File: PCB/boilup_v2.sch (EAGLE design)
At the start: 36 parts, among them IC1 THS4211, J1 USB-MICROB, U1 STM32F0_LQFP64, U2 SPX3819-3.3

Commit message: Added V2 brd layout
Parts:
- removed J1: USB-MICROB, SparkFun-Connectors:USB-MICROB
- removed JP2: (no value), pinhead:PINHD-2X5
- added C4: 100uF, resistor:C-EUC1210K
- added C5: 10uF, resistor:C-EUC0603K
- added H3: MOUNT-HOLE2.8, holes:MOUNT-HOLE2.8
- added JP1: (no value), pinhead:PINHD-1X2
- added LED3: (no value), led:LEDSML0805
- added R12: (no value), resistor:R-US_R0603
- added REDUDNAT: (no value), pinhead:PINHD-2X5
- added U$3: TPSM842, smarttle:TPSM842
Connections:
- removed net D+: J1.D+
- removed net D-: J1.D-
- new net +12V: C5.1, D1.C, JP1.2, MOT.1, U$3.VIN
- new net N$5: LED3.A, R12.1
- net +3V3: no longer IC1G$1.V+
- net +5V: now also C4.1, IC1G$1.V+, REDUDNAT.1, U$3.VOUT; no longer D1.C, J1.VBUS, JP2.1, MOT.1
- net DAC: now also REDUDNAT.3; no longer JP2.3
- net GND: now also C4.2, C5.2, JP1.1, LED3.C, REDUDNAT.10, U$3.GND; no longer J1.GND, JP2.10
- net MOSI: no longer JP2.7
- net PUSH_BUTT: now also R12.2, REDUDNAT.8; no longer JP2.8
- net SCK: no longer JP2.5
- net TIM2_CH3: now also REDUDNAT.9; no longer JP2.9
- net TIM2_CH4: now also REDUDNAT.6; no longer JP2.6
- net USART_RX: now also REDUDNAT.2; no longer JP2.2
- net USART_TX: now also REDUDNAT.4; no longer JP2.4
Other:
- note added: "change to 5?"
- note removed: "POWER AND PORTS"
- moved on the sheet: R1

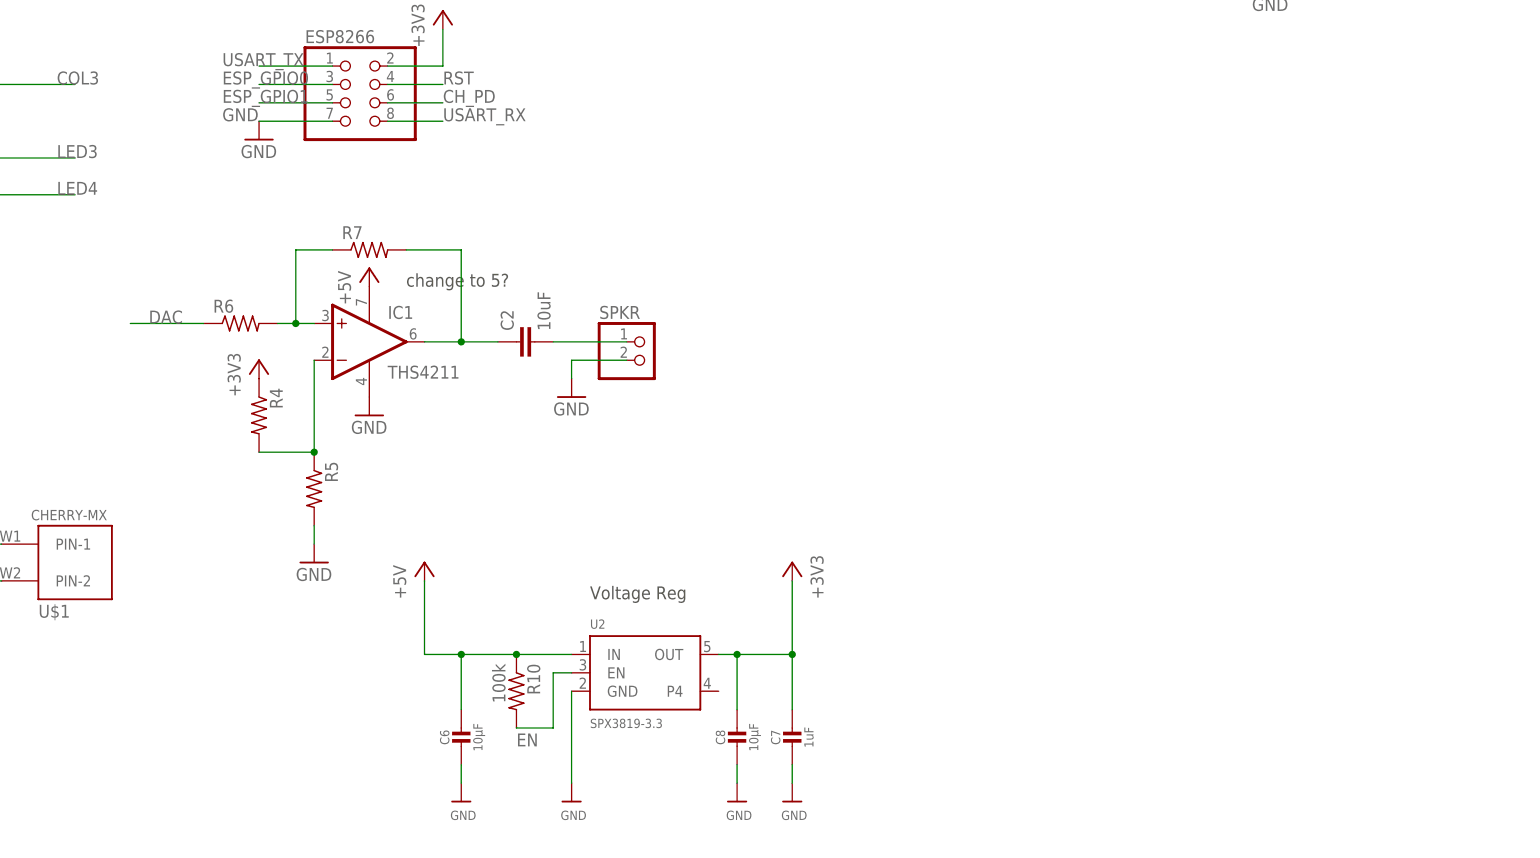
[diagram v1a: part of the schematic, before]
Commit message: replaced speaker circuit, redid board layout. V2 is active development version
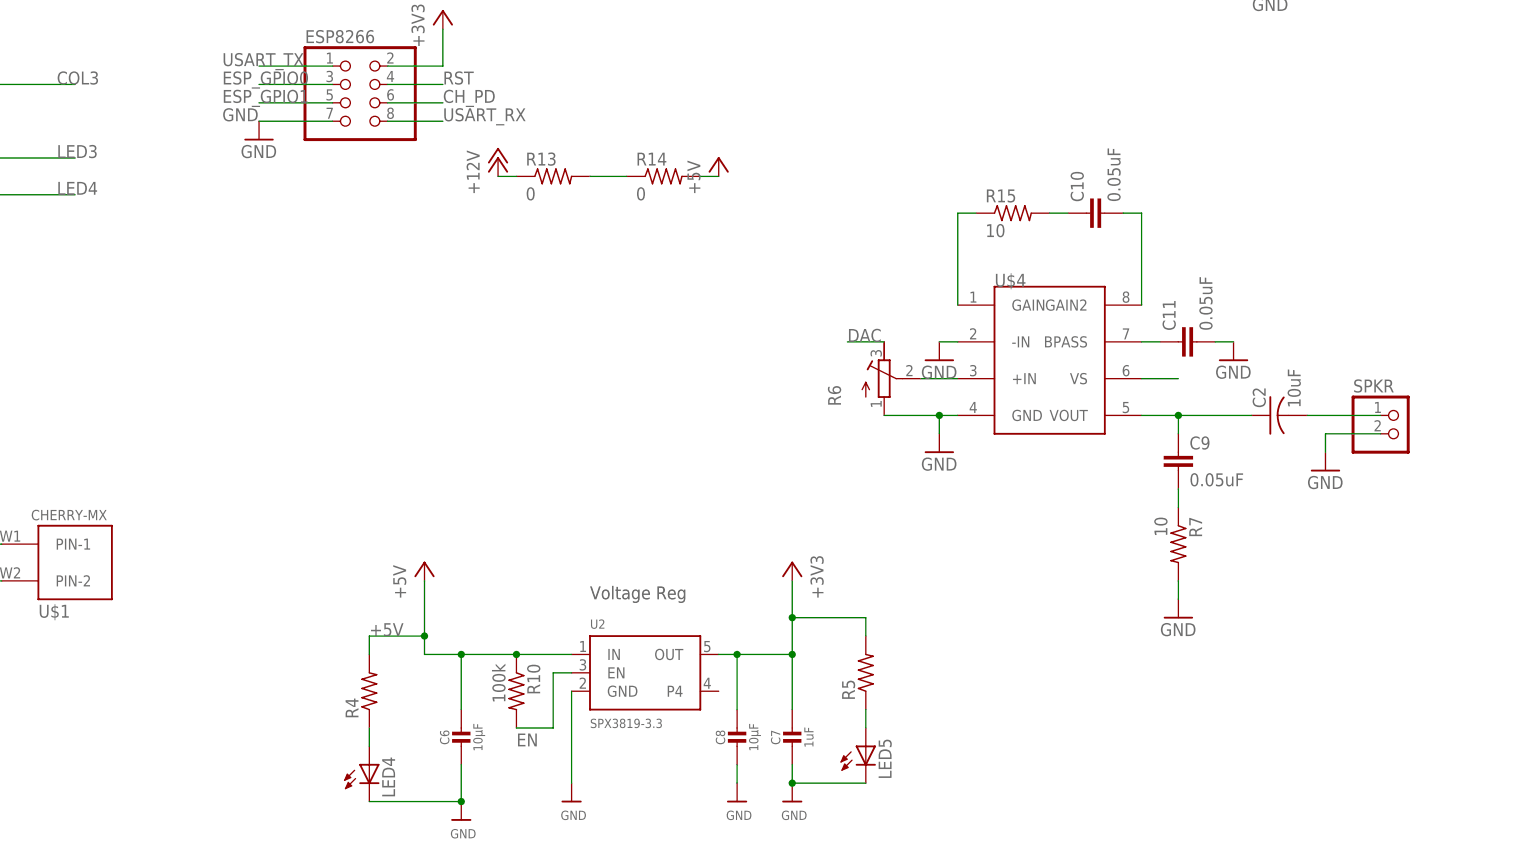
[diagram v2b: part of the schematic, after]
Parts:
- removed IC1: THS4211, texas:THS4211
- added C10, C11, C9: 0.05uF, resistor:C-EUC0603K
- added LED4, LED5: (no value), led:LEDSML0805
- added R13, R14: 0, resistor:R-US_R0603
- added R15: 10, resistor:R-US_R0603
- added U$4: LM386, smarttle:LM386
- C2: device resistor:C-EUC0603K -> resistor:C-USC1210K
- R6: device resistor:R-US_R0603 -> resistor:R-TRIMM3224X
- R7: value (none) -> 10
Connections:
- removed net AMP: IC1G$1.+IN, R6.2, R7.1
- removed net N$17: C2.1, IC1G$1.OUT, R7.2
- new net N$10: R15.1, U$4.GAIN
- new net N$11: C10.2, U$4.GAIN2
- new net N$12: C10.1, R15.2
- new net N$13: C11.1, U$4.BPASS
- new net N$14: LED5.A, R5.1
- new net N$6: C9.2, R7.1
- new net N$8: C2.1, C9.1, U$4.VOUT
- new net N$9: R6.S, U$4.+IN
- new net OPAMPSUPPLY: R13.2, R14.1, U$4.VS
- net +12V: now also R13.1
- net +3V3: now also R5.2; no longer R4.1
- net +5V: now also R14.2, R4.2; no longer IC1G$1.V+
- net DAC: now also R6.E; no longer R6.1
- net GND: now also C11.2, LED4.C, LED5.C, R6.A, R7.2, U$4.-IN, U$4.GND; no longer IC1G$1.V-, R5.2
- net N$7: now also LED4.A, R4.1; no longer IC1G$1.-IN, R4.2, R5.1
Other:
- note removed: "change to 5?"
- moved on the sheet: C2, R4, R5, R7, SPKR

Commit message: More small updates. check v2
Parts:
- renumbered LED3 to BUTTON, LED4 to 5V, LED5 to 3V3, REDUDNAT to REDUNDANT
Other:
- note added: "Micro controlled LEDs"
- note added: "MicroController Power and Config"
- note added: "Power Conversion"
- note added: "Power Selection speaker Driver"
- note added: "Speaker Driver"
- moved on the sheet: R13, R14
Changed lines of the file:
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@@
 <part name="C1" library="microbuilder" deviceset="CAP_CERAMIC" device="0805-NOOUTLINE" value="10nF"/>
 <part name="C3" library="microbuilder" deviceset="CAP_CERAMIC" device="0805-NOOUTLINE" value="10nF"/>
-<part name="REDUDNAT" library="pinhead" library_urn="urn:adsk.eagle:library:325" deviceset="PINHD-2X5" device="" package3d_urn="urn:adsk.eagle:package:22470/2"/>
-<part name="LED3" library="led" library_urn="urn:adsk.eagle:library:259" deviceset="LED" device="SML0805" package3d_urn="urn:adsk.eagle:package:15830/1"/>
+<part name="REDUNDANT" library="pinhead" library_urn="urn:adsk.eagle:library:325" deviceset="PINHD-2X5" device="" package3d_urn="urn:adsk.eagle:package:22470/2"/>
+<part name="BUTTON" library="led" library_urn="urn:adsk.eagle:library:259" deviceset="LED" device="SML0805" package3d_urn="urn:adsk.eagle:package:15830/1"/>
 <part name="R12" library="resistor" library_urn="urn:adsk.eagle:library:348" deviceset="R-US_" device="R0603" package3d_urn="urn:adsk.eagle:package:26057/1"/>
 <part name="U$3" library="smarttle" deviceset="TPSM842" device=""/>
@@
 <part name="C11" library="resistor" library_urn="urn:adsk.eagle:library:348" deviceset="C-EU" device="C0603K" package3d_urn="urn:adsk.eagle:package:26200/1" value="0.05uF"/>
 <part name="GND12" library="supply1" library_urn="urn:adsk.eagle:library:371" deviceset="GND" device=""/>
-<part name="LED4" library="led" library_urn="urn:adsk.eagle:library:259" deviceset="LED" device="SML0805" package3d_urn="urn:adsk.eagle:package:15830/1"/>
+<part name="5V" library="led" library_urn="urn:adsk.eagle:library:259" deviceset="LED" device="SML0805" package3d_urn="urn:adsk.eagle:package:15830/1"/>
 <part name="R4" library="resistor" library_urn="urn:adsk.eagle:library:348" deviceset="R-US_" device="R0603" package3d_urn="urn:adsk.eagle:package:26057/1"/>
-<part name="LED5" library="led" library_urn="urn:adsk.eagle:library:259" deviceset="LED" device="SML0805" package3d_urn="urn:adsk.eagle:package:15830/1"/>
+<part name="3V3" library="led" library_urn="urn:adsk.eagle:library:259" deviceset="LED" device="SML0805" package3d_urn="urn:adsk.eagle:package:15830/1"/>
 <part name="R5" library="resistor" library_urn="urn:adsk.eagle:library:348" deviceset="R-US_" device="R0603" package3d_urn="urn:adsk.eagle:package:26057/1"/>
 </parts>
@@
 <text x="170.18" y="187.96" size="1.778" layer="97">5V @ .2A</text>
 <text x="167.64" y="53.34" size="1.778" layer="97">Voltage Reg</text>
+<text x="20.32" y="116.84" size="1.778" layer="97">MicroController Power and Config</text>
+<text x="251.46" y="162.56" size="1.778" layer="97">Power Conversion</text>
+<text x="233.68" y="116.84" size="1.778" layer="97">Speaker Driver</text>
+<text x="30.48" y="71.12" size="1.778" layer="97">Micro controlled LEDs</text>
+<text x="254" y="111.76" size="1.778" layer="97">Power Selection speaker Driver</text>
 </plain>
 <instances>
@@
 <instance part="C1" gate="G$1" x="55.88" y="93.98"/>
 <instance part="C3" gate="G$1" x="63.5" y="93.98"/>
-<instance part="REDUDNAT" gate="A" x="210.82" y="236.22"/>
-<instance part="LED3" gate="G$1" x="71.12" y="40.64"/>
+<instance part="REDUNDANT" gate="A" x="210.82" y="236.22"/>
+<instance part="BUTTON" gate="G$1" x="71.12" y="40.64"/>
 <instance part="R12" gate="G$1" x="71.12" y="48.26" rot="R90"/>
 <instance part="U$3" gate="G$1" x="261.62" y="154.94"/>
@@
 <instance part="P+1" gate="1" x="149.86" y="198.12"/>
 <instance part="H3" gate="G$1" x="287.02" y="233.68"/>
-<instance part="R13" gate="G$1" x="162.56" y="111.76"/>
-<instance part="R14" gate="G$1" x="177.8" y="111.76"/>
-<instance part="P+3" gate="1" x="154.94" y="114.3"/>
-<instance part="P+5" gate="1" x="185.42" y="114.3"/>
+<instance part="R13" gate="G$1" x="264.16" y="104.14"/>
+<instance part="R14" gate="G$1" x="279.4" y="104.14"/>
+<instance part="P+3" gate="1" x="256.54" y="106.68"/>
+<instance part="P+5" gate="1" x="287.02" y="106.68"/>
 <instance part="U$4" gate="G$1" x="231.14" y="86.36"/>
 <instance part="C9" gate="G$1" x="248.92" y="73.66"/>
@@
 <instance part="C11" gate="G$1" x="248.92" y="88.9" rot="R90"/>
 <instance part="GND12" gate="1" x="256.54" y="86.36"/>
-<instance part="LED4" gate="G$1" x="137.16" y="30.48"/>
+<instance part="5V" gate="G$1" x="137.16" y="30.48"/>
 <instance part="R4" gate="G$1" x="137.16" y="40.64" rot="R90"/>
-<instance part="LED5" gate="G$1" x="205.74" y="33.02"/>
+<instance part="3V3" gate="G$1" x="205.74" y="33.02"/>
 <instance part="R5" gate="G$1" x="205.74" y="43.18" rot="R90"/>
 </instances>
@@
 </segment>
 <segment>
-<pinref part="REDUDNAT" gate="A" pin="4"/>
+<pinref part="REDUNDANT" gate="A" pin="4"/>
 <wire x1="215.9" y1="238.76" x2="220.98" y2="238.76" width="0.1524" layer="91"/>
 <label x="220.98" y="238.76" size="1.778" layer="95"/>
@@
 <pinref part="R1" gate="G$1" pin="1"/>
 <wire x1="81.28" y1="33.02" x2="81.28" y2="38.1" width="0.1524" layer="91"/>
-<pinref part="LED3" gate="G$1" pin="C"/>
+<pinref part="BUTTON" gate="G$1" pin="C"/>
 <wire x1="71.12" y1="35.56" x2="81.28" y2="35.56" width="0.1524" layer="91"/>
 <wire x1="81.28" y1="35.56" x2="81.28" y2="33.02" width="0.1524" layer="91"/>
@@
 <pinref part="U$28" gate="G$1" pin="GND"/>
 <wire x1="195.58" y1="30.48" x2="195.58" y2="27.94" width="0.1524" layer="91"/>
-<pinref part="LED5" gate="G$1" pin="C"/>
+<pinref part="3V3" gate="G$1" pin="C"/>
 <wire x1="205.74" y1="27.94" x2="195.58" y2="27.94" width="0.1524" layer="91"/>
 <junction x="195.58" y="27.94"/>
@@
 <pinref part="U$27" gate="G$1" pin="GND"/>
 <wire x1="149.86" y1="30.48" x2="149.86" y2="25.4" width="0.1524" layer="91"/>
-<pinref part="LED4" gate="G$1" pin="C"/>
+<pinref part="5V" gate="G$1" pin="C"/>
 <wire x1="149.86" y1="25.4" x2="137.16" y2="25.4" width="0.1524" layer="91"/>
 <junction x="149.86" y="25.4"/>
@@
 </segment>
 <segment>
-<pinref part="REDUDNAT" gate="A" pin="10"/>
+<pinref part="REDUNDANT" gate="A" pin="10"/>
 <wire x1="215.9" y1="231.14" x2="223.52" y2="231.14" width="0.1524" layer="91"/>
 <label x="220.98" y="231.14" size="1.778" layer="95"/>
@@
 </segment>
 <segment>
-<pinref part="REDUDNAT" gate="A" pin="1"/>
+<pinref part="REDUNDANT" gate="A" pin="1"/>
 <wire x1="208.28" y1="241.3" x2="200.66" y2="241.3" width="0.1524" layer="91"/>
 <label x="198.12" y="241.3" size="1.778" layer="95"/>
@@
 <pinref part="R14" gate="G$1" pin="2"/>
 <pinref part="P+5" gate="1" pin="+5V"/>
-<wire x1="182.88" y1="111.76" x2="185.42" y2="111.76" width="0.1524" layer="91"/>
+<wire x1="284.48" y1="104.14" x2="287.02" y2="104.14" width="0.1524" layer="91"/>
 </segment>
 </net>
@@
 </segment>
 <segment>
-<pinref part="REDUDNAT" gate="A" pin="8"/>
+<pinref part="REDUNDANT" gate="A" pin="8"/>
 <wire x1="215.9" y1="233.68" x2="223.52" y2="233.68" width="0.1524" layer="91"/>
 <label x="220.98" y="233.68" size="1.778" layer="95"/>
@@
 </segment>
 <segment>
-<pinref part="REDUDNAT" gate="A" pin="9"/>
+<pinref part="REDUNDANT" gate="A" pin="9"/>
 <wire x1="208.28" y1="231.14" x2="200.66" y2="231.14" width="0.1524" layer="91"/>
 <label x="193.04" y="231.14" size="1.778" layer="95"/>
@@
 </segment>
 <segment>
-<pinref part="REDUDNAT" gate="A" pin="6"/>
+<pinref part="REDUNDANT" gate="A" pin="6"/>
 <wire x1="215.9" y1="236.22" x2="223.52" y2="236.22" width="0.1524" layer="91"/>
 <label x="220.98" y="236.22" size="1.778" layer="95"/>
@@
 </segment>
 <segment>
-<pinref part="REDUDNAT" gate="A" pin="3"/>
+<pinref part="REDUNDANT" gate="A" pin="3"/>
 <wire x1="208.28" y1="238.76" x2="200.66" y2="238.76" width="0.1524" layer="91"/>
 <label x="198.12" y="238.76" size="1.778" layer="95"/>
@@
 </segment>
 <segment>
-<pinref part="REDUDNAT" gate="A" pin="2"/>
+<pinref part="REDUNDANT" gate="A" pin="2"/>
 <wire x1="215.9" y1="241.3" x2="220.98" y2="241.3" width="0.1524" layer="91"/>
 <label x="220.98" y="241.3" size="1.778" layer="95"/>
@@
 <net name="N$5" class="0">
 <segment>
-<pinref part="LED3" gate="G$1" pin="A"/>
+<pinref part="BUTTON" gate="G$1" pin="A"/>
 <pinref part="R12" gate="G$1" pin="1"/>
 </segment>
@@
 <pinref part="R13" gate="G$1" pin="1"/>
 <pinref part="P+3" gate="1" pin="+12V"/>
-<wire x1="157.48" y1="111.76" x2="154.94" y2="111.76" width="0.1524" layer="91"/>
+<wire x1="259.08" y1="104.14" x2="256.54" y2="104.14" width="0.1524" layer="91"/>
 </segment>
 </net>
@@
 <pinref part="R13" gate="G$1" pin="2"/>
 <pinref part="R14" gate="G$1" pin="1"/>
-<wire x1="167.64" y1="111.76" x2="172.72" y2="111.76" width="0.1524" layer="91"/>
+<wire x1="269.24" y1="104.14" x2="274.32" y2="104.14" width="0.1524" layer="91"/>
 </segment>
 <segment>
@@
 <net name="N$7" class="0">
 <segment>
-<pinref part="LED4" gate="G$1" pin="A"/>
+<pinref part="5V" gate="G$1" pin="A"/>
 <pinref part="R4" gate="G$1" pin="1"/>
 <wire x1="137.16" y1="35.56" x2="137.16" y2="33.02" width="0.1524" layer="91"/>
@@
 <net name="N$14" class="0">
 <segment>
-<pinref part="LED5" gate="G$1" pin="A"/>
+<pinref part="3V3" gate="G$1" pin="A"/>
 <pinref part="R5" gate="G$1" pin="1"/>
 <wire x1="205.74" y1="38.1" x2="205.74" y2="35.56" width="0.1524" layer="91"/>
